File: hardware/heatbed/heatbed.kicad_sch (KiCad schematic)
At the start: 6 parts, among them J1 Conn_01x01, J2 Conn_01x01

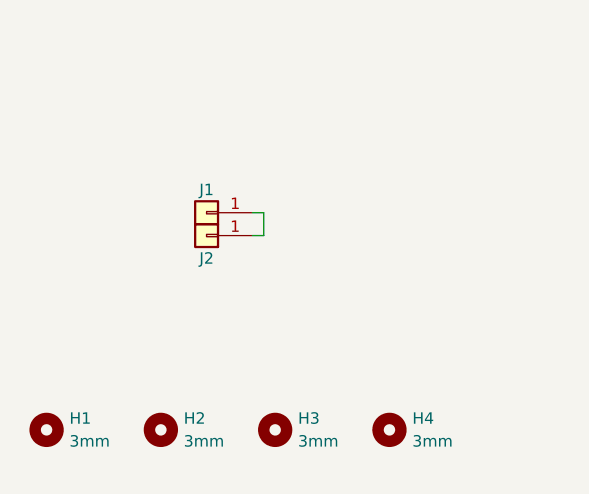
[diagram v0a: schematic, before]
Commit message: Improve hot plate PCB design
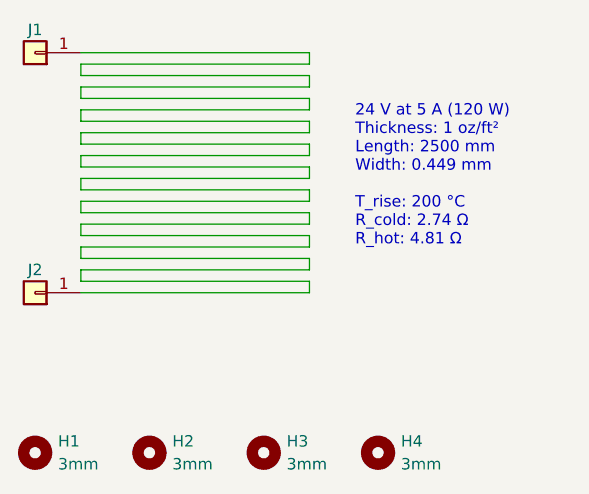
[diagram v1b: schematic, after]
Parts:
- H1, H2, H3, H4: now left out of the parts list
- J1, J2: footprint Connector_Pin:Pin_D1.3mm_L11.0mm -> Local_Library:Pogo_Pad; now left out of the parts list
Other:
- note added: "24 V at 5 A (120 W) Thickness: 1 oz/ft² Length: 2500 mm Width: 0.449 mm T_rise: 200 °C R_cold: 2.74 Ω R_hot: 4.81 Ω"
- moved on the sheet: H1, H2, H3, H4, J1, J2

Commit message: Use one-sided pads
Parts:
- H1, H2, H3, H4: footprint MountingHole:MountingHole_3mm -> Local_Library:MountingHole_3mm
- J1, J2: footprint Local_Library:Pogo_Pad -> Local_Library:Pad_D3mm_H0.4mm
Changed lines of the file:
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@@
       (effects (font (size 1.27 1.27)) hide)
     )
-    (property "Footprint" "Local_Library:Pogo_Pad" (at 125.73 107.95 0)
+    (property "Footprint" "Local_Library:Pad_D3mm_H0.4mm" (at 125.73 107.95 0)
       (effects (font (size 1.27 1.27)) hide)
     )
@@
       (effects (font (size 1.27 1.27)) (justify left))
     )
-    (property "Footprint" "MountingHole:MountingHole_3mm" (at 163.83 125.73 0)
+    (property "Footprint" "Local_Library:MountingHole_3mm" (at 163.83 125.73 0)
       (effects (font (size 1.27 1.27)) hide)
     )
@@
       (effects (font (size 1.27 1.27)) hide)
     )
-    (property "Footprint" "Local_Library:Pogo_Pad" (at 125.73 81.28 0)
+    (property "Footprint" "Local_Library:Pad_D3mm_H0.4mm" (at 125.73 81.28 0)
       (effects (font (size 1.27 1.27)) hide)
     )
@@
       (effects (font (size 1.27 1.27)) (justify left))
     )
-    (property "Footprint" "MountingHole:MountingHole_3mm" (at 125.73 125.73 0)
+    (property "Footprint" "Local_Library:MountingHole_3mm" (at 125.73 125.73 0)
       (effects (font (size 1.27 1.27)) hide)
     )
@@
       (effects (font (size 1.27 1.27)) (justify left))
     )
-    (property "Footprint" "MountingHole:MountingHole_3mm" (at 138.43 125.73 0)
+    (property "Footprint" "Local_Library:MountingHole_3mm" (at 138.43 125.73 0)
       (effects (font (size 1.27 1.27)) hide)
     )
@@
       (effects (font (size 1.27 1.27)) (justify left))
     )
-    (property "Footprint" "MountingHole:MountingHole_3mm" (at 151.13 125.73 0)
+    (property "Footprint" "Local_Library:MountingHole_3mm" (at 151.13 125.73 0)
       (effects (font (size 1.27 1.27)) hide)
     )

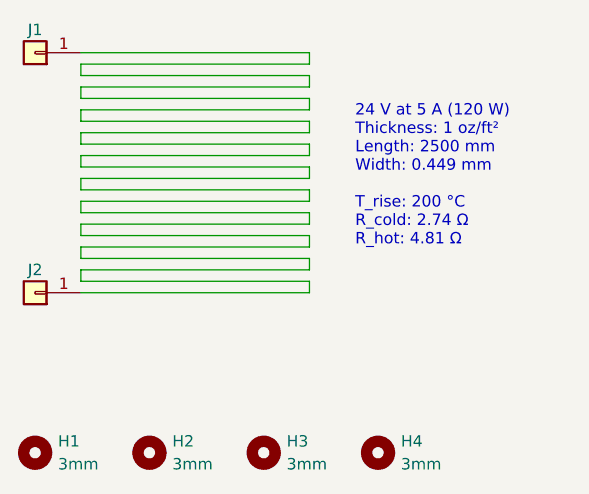
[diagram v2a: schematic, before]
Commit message: Change mounting holes to M2.5 and use ring terminals
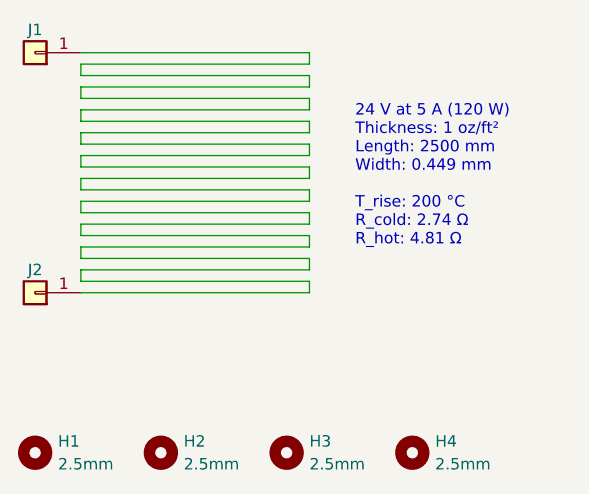
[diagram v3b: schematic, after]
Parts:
- H1, H2, H3, H4: value 3mm -> 2.5mm; footprint Local_Library:MountingHole_3mm -> Local_Library:MountingHole_2.5mm
- J1, J2: footprint Local_Library:Pad_D3mm_H0.4mm -> Local_Library:Pad_D5mm_H2.2mm
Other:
- moved on the sheet: H2, H3, H4
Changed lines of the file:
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@@
   (title_block
     (title "Reflow Hot Plate Heatbed")
-    (date "2023-07-15")
+    (date "2023-07-31")
     (rev "${REVISION}")
     (company "Author: I. Kajdan")
@@
       (effects (font (size 1.27 1.27)) hide)
     )
-    (property "Footprint" "Local_Library:Pad_D3mm_H0.4mm" (at 125.73 107.95 0)
+    (property "Footprint" "Local_Library:Pad_D5mm_H2.2mm" (at 125.73 107.95 0)
       (effects (font (size 1.27 1.27)) hide)
     )
@@
     )
   )
-  (symbol (lib_id "Mechanical:MountingHole") (at 163.83 125.73 0) (unit 1)
-    (in_bom no) (on_board yes) (dnp no) (fields_autoplaced)
-    (property "Reference" "H4" (at 166.37 124.46 0)
-      (effects (font (size 1.27 1.27)) (justify left))
-    )
-    (property "Value" "3mm" (at 166.37 127 0)
-      (effects (font (size 1.27 1.27)) (justify left))
-    )
-    (property "Footprint" "Local_Library:MountingHole_3mm" (at 163.83 125.73 0)
-      (effects (font (size 1.27 1.27)) hide)
-    )
-    (property "Datasheet" "~" (at 163.83 125.73 0)
+  (symbol (lib_id "Mechanical:MountingHole") (at 167.64 125.73 0) (unit 1)
+    (in_bom no) (on_board yes) (dnp no) (fields_autoplaced)
+    (property "Reference" "H4" (at 170.18 124.46 0)
+      (effects (font (size 1.27 1.27)) (justify left))
+    )
+    (property "Value" "2.5mm" (at 170.18 127 0)
+      (effects (font (size 1.27 1.27)) (justify left))
+    )
+    (property "Footprint" "Local_Library:MountingHole_2.5mm" (at 167.64 125.73 0)
+      (effects (font (size 1.27 1.27)) hide)
+    )
+    (property "Datasheet" "~" (at 167.64 125.73 0)
       (effects (font (size 1.27 1.27)) hide)
     )
@@
       (effects (font (size 1.27 1.27)) hide)
     )
-    (property "Footprint" "Local_Library:Pad_D3mm_H0.4mm" (at 125.73 81.28 0)
+    (property "Footprint" "Local_Library:Pad_D5mm_H2.2mm" (at 125.73 81.28 0)
       (effects (font (size 1.27 1.27)) hide)
     )
@@
       (effects (font (size 1.27 1.27)) (justify left))
     )
-    (property "Value" "3mm" (at 128.27 127 0)
-      (effects (font (size 1.27 1.27)) (justify left))
-    )
-    (property "Footprint" "Local_Library:MountingHole_3mm" (at 125.73 125.73 0)
+    (property "Value" "2.5mm" (at 128.27 127 0)
+      (effects (font (size 1.27 1.27)) (justify left))
+    )
+    (property "Footprint" "Local_Library:MountingHole_2.5mm" (at 125.73 125.73 0)
       (effects (font (size 1.27 1.27)) hide)
     )
@@
     )
   )
-  (symbol (lib_id "Mechanical:MountingHole") (at 138.43 125.73 0) (unit 1)
-    (in_bom no) (on_board yes) (dnp no) (fields_autoplaced)
-    (property "Reference" "H2" (at 140.97 124.46 0)
-      (effects (font (size 1.27 1.27)) (justify left))
-    )
-    (property "Value" "3mm" (at 140.97 127 0)
-      (effects (font (size 1.27 1.27)) (justify left))
-    )
-    (property "Footprint" "Local_Library:MountingHole_3mm" (at 138.43 125.73 0)
-      (effects (font (size 1.27 1.27)) hide)
-    )
-    (property "Datasheet" "~" (at 138.43 125.73 0)
+  (symbol (lib_id "Mechanical:MountingHole") (at 139.7 125.73 0) (unit 1)
+    (in_bom no) (on_board yes) (dnp no) (fields_autoplaced)
+    (property "Reference" "H2" (at 142.24 124.46 0)
+      (effects (font (size 1.27 1.27)) (justify left))
+    )
+    (property "Value" "2.5mm" (at 142.24 127 0)
+      (effects (font (size 1.27 1.27)) (justify left))
+    )
+    (property "Footprint" "Local_Library:MountingHole_2.5mm" (at 139.7 125.73 0)
+      (effects (font (size 1.27 1.27)) hide)
+    )
+    (property "Datasheet" "~" (at 139.7 125.73 0)
       (effects (font (size 1.27 1.27)) hide)
     )
@@
     )
   )
-  (symbol (lib_id "Mechanical:MountingHole") (at 151.13 125.73 0) (unit 1)
-    (in_bom no) (on_board yes) (dnp no) (fields_autoplaced)
-    (property "Reference" "H3" (at 153.67 124.46 0)
-      (effects (font (size 1.27 1.27)) (justify left))
-    )
-    (property "Value" "3mm" (at 153.67 127 0)
-      (effects (font (size 1.27 1.27)) (justify left))
-    )
-    (property "Footprint" "Local_Library:MountingHole_3mm" (at 151.13 125.73 0)
-      (effects (font (size 1.27 1.27)) hide)
-    )
-    (property "Datasheet" "~" (at 151.13 125.73 0)
-      (effects (font (size 1.27 1.27)) hide)
-    )
+  (symbol (lib_id "Mechanical:MountingHole") (at 153.67 125.73 0) (unit 1)
+    (in_bom no) (on_board yes) (dnp no) (fields_autoplaced)
+    (property "Reference" "H3" (at 156.21 124.46 0)
+      (effects (font (size 1.27 1.27)) (justify left))
+    )
+    (property "Value" "2.5mm" (at 156.21 127 0)
+      (effects (font (size 1.27 1.27)) (justify left))
+    )
+    (property "Footprint" "Local_Library:MountingHole_2.5mm" (at 153.67 125.73 0)
+      (effects (font (size 1.27 1.27)) hide)
+    )
+    (property "Datasheet" "~" (at 153.67 125.73 0)
+      (effects (font (size 1.27 1.27)) hide)
+    )

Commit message: Remove mounting hole silkscreen circles
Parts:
- H1, H2, H3, H4: footprint Local_Library:MountingHole_2.5mm -> MountingHole:MountingHole_2.5mm
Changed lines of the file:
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@@
   (title_block
     (title "Reflow Hot Plate Heatbed")
-    (date "2023-07-31")
+    (date "2023-08-09")
     (rev "${REVISION}")
     (company "Author: I. Kajdan")
@@
       (effects (font (size 1.27 1.27)) (justify left))
     )
-    (property "Footprint" "Local_Library:MountingHole_2.5mm" (at 167.64 125.73 0)
+    (property "Footprint" "MountingHole:MountingHole_2.5mm" (at 167.64 125.73 0)
       (effects (font (size 1.27 1.27)) hide)
     )
@@
       (effects (font (size 1.27 1.27)) (justify left))
     )
-    (property "Footprint" "Local_Library:MountingHole_2.5mm" (at 125.73 125.73 0)
+    (property "Footprint" "MountingHole:MountingHole_2.5mm" (at 125.73 125.73 0)
       (effects (font (size 1.27 1.27)) hide)
     )
@@
       (effects (font (size 1.27 1.27)) (justify left))
     )
-    (property "Footprint" "Local_Library:MountingHole_2.5mm" (at 139.7 125.73 0)
+    (property "Footprint" "MountingHole:MountingHole_2.5mm" (at 139.7 125.73 0)
       (effects (font (size 1.27 1.27)) hide)
     )
@@
       (effects (font (size 1.27 1.27)) (justify left))
     )
-    (property "Footprint" "Local_Library:MountingHole_2.5mm" (at 153.67 125.73 0)
-      (effects (font (size 1.27 1.27)) hide)
-    )
+    (property "Footprint" "MountingHole:MountingHole_2.5mm" (at 153.67 125.73 0)
+      (effects (font (size 1.27 1.27)) hide)
+    )
